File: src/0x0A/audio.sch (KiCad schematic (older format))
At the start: 2 parts

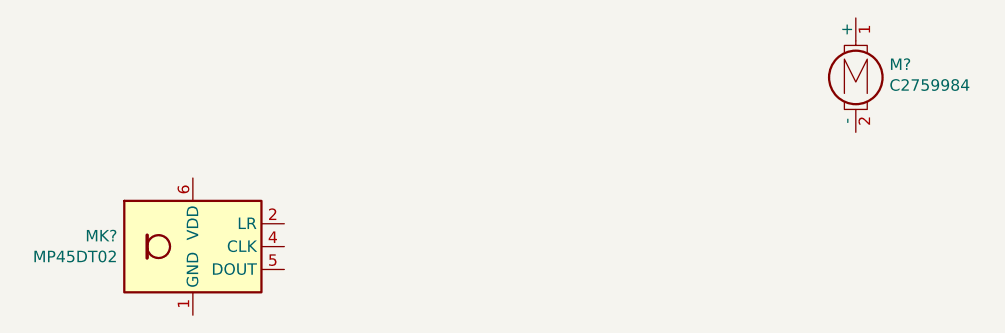
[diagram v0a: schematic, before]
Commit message: new file:   imgs/better.png 	modified:   src/0x0A/0x0A-cache.lib 	modified:   src/0x0A/0x0A.sch 	modified:   src/0x0A/antenna.sch 	modified:   src/0x0A/audio.sch 	modified:   src/0x0A/buttons.sch 	new file:   src/0x0A/cameras.sch 	modified:   src/0x0A/display.sch 	modified:   src/0x0A/gpio.sch 	modified:   src/0x0A/pwr.sch 	modified:   src/0x0A/sensors.sch 	modified:   src/0x0A/sim.sch 	modified:   src/0x0A/uart.sch 	modified:   src/0x0A/usb.sch 	new file:   src/models/body.obj 	new file:   src/models/phone.FCStd 	new file:   src/models/screen.obj
Added 3D models, integrated front & rear cameras, flash light, reformatting & more
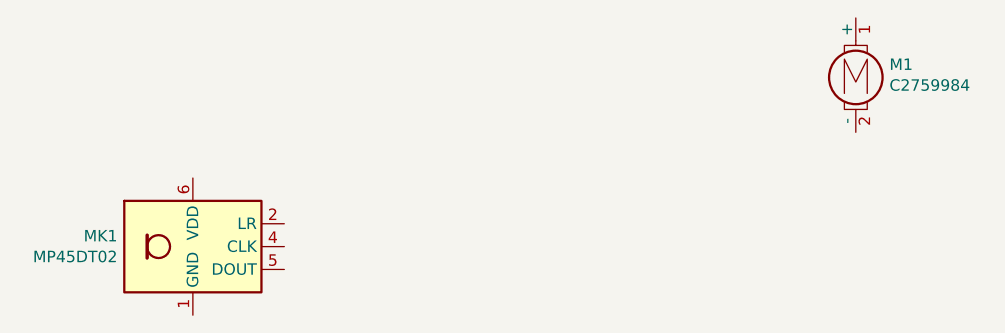
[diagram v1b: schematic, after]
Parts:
- gave numbers to parts that had none: 2
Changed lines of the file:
@@
 $Descr A4 11693 8268
 encoding utf-8
-Sheet 9 12
+Sheet 9 13
 Title "0x0A SmartPhone"
 Date "2022-09-01"
 Rev "1"
 Comp "HackThisPhone.com"
-Comment1 ""
+Comment1 "Designed By @NoahGWood for"
 Comment2 ""
 Comment3 ""
@@
 $EndDescr
 $Comp
-L Sensor_Audio:MP45DT02 MK?
+L Sensor_Audio:MP45DT02 MK1
 U 1 1 63F66D5E
 P 4050 3350
-F 0 "MK?" H 3720 3396 50  0000 R CNN
+F 0 "MK1" H 3720 3396 50  0000 R CNN
 F 1 "MP45DT02" H 3720 3305 50  0000 R CNN
 F 2 "Sensor_Audio:ST_HLGA-6_3.76x4.72mm_P1.65mm" H 3150 3000 50  0001 L CIN
@@
 $EndComp
 $Comp
-L Motor:Motor_DC_ALT M?
+L Motor:Motor_DC_ALT M1
 U 1 1 63FA151C
 P 6950 2550
-F 0 "M?" H 7097 2546 50  0000 L CNN
+F 0 "M1" H 7097 2546 50  0000 L CNN
 F 1 "C2759984" H 7097 2455 50  0000 L CNN
 F 2 "" H 6950 2460 50  0001 C CNN

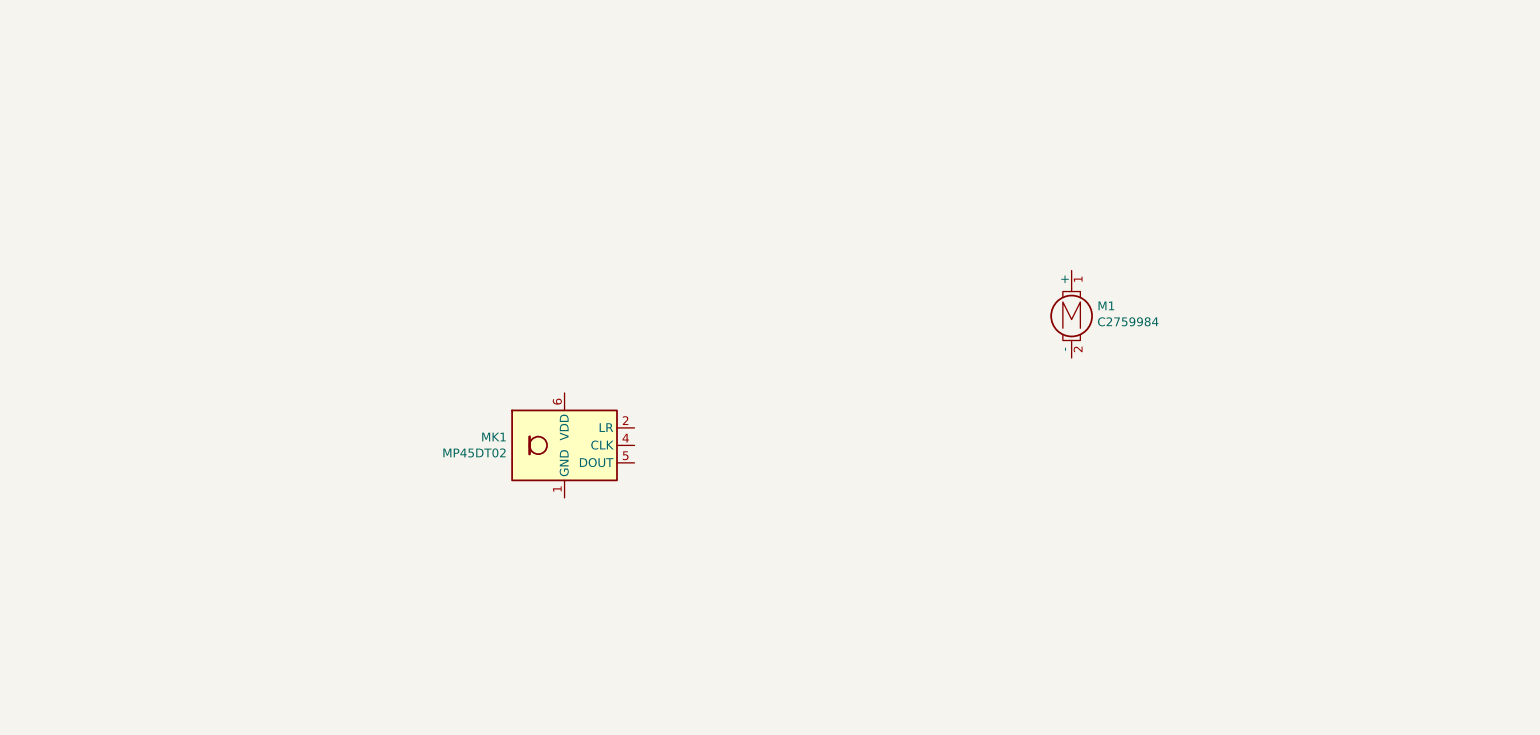
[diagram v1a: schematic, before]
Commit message: Updated schematics, started working on board layout
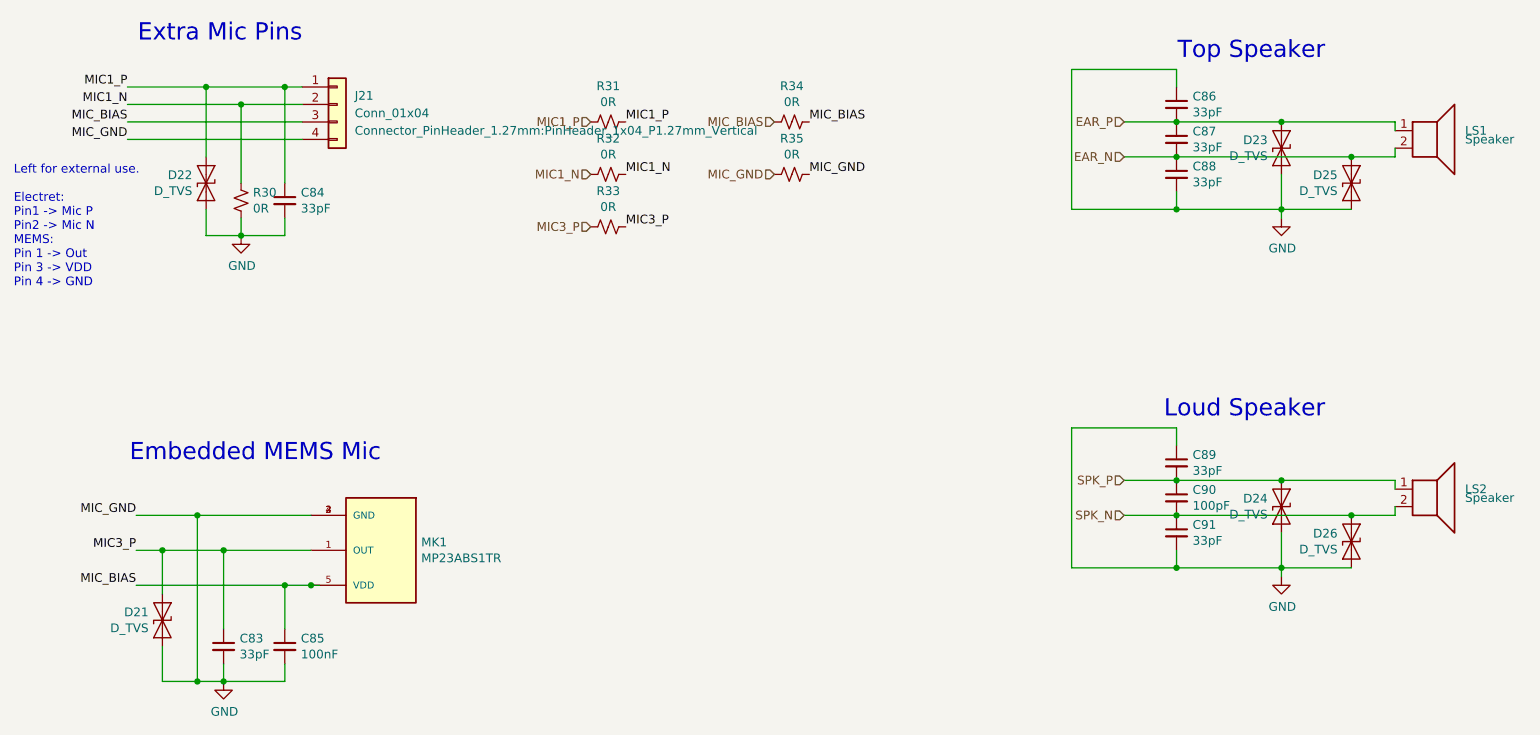
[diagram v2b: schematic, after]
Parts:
- removed M1: C2759984, symbol Motor:Motor_DC_ALT
- removed MK1: MP45DT02, Sensor_Audio:ST_HLGA-6_3.76x4.72mm_P1.65mm, symbol Sensor_Audio:MP45DT02
- added C83, C84, C86, C87, C88, C89, C91: 33pF, Capacitor_SMD:C_0603_1608Metric, symbol Device:C_Small
- added C85: 100nF, Capacitor_SMD:C_0402_1005Metric, symbol Device:C_Small
- added C90: 100pF, Capacitor_SMD:C_0603_1608Metric, symbol Device:C_Small
- added D21, D22, D23, D24, D25, D26: D_TVS, symbol Device:D_TVS
- added J21: Conn_01x04, Connector_PinHeader_1.27mm:PinHeader_1x04_P1.27mm_Vertical, symbol Connector_Generic:Conn_01x04
- added LS1, LS2: Speaker, Connector_PinHeader_1.27mm:PinHeader_1x02_P1.27mm_Horizontal, symbol Device:Speaker
- added MK1: MP23ABS1TR, SnapEDA Library:MIC_MP23ABS1TR, symbol MP23ABS1TR:MP23ABS1TR
- added R30, R31, R32, R33, R34, R35: 0R, Resistor_SMD:R_0402_1005Metric, symbol Device:R_Small_US
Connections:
- new net EAR_N: C87.2, C88.1, D25.2 (A2), LS1.2
- new net EAR_P: C86.2, C87.1, D23.2 (A2), LS1.1
- new net GND: C83.2, C84.2, C85.2, C86.1, C88.2, C89.1, C91.2, D21.1 (A1), D22.1 (A1), D23.1 (A1), D24.1 (A1), D25.1 (A1), D26.1 (A1), J21.4 (Pin_4), MK1.2 (GND), MK1.3 (GND), MK1.4 (GND), R30.1, R35.1, R35.2
- new net MIC1_N: J21.2 (Pin_2), R30.2, R32.1, R32.2
- new net MIC1_P: C84.1, D22.2 (A2), J21.1 (Pin_1), R31.1, R31.2
- new net MIC3_P: C83.1, D21.2 (A2), MK1.1 (OUT), R33.1, R33.2
- new net MIC_BIAS: C85.1, J21.3 (Pin_3), MK1.5 (VDD), R34.1, R34.2
- new net SPK_N: C90.2, C91.1, D26.2 (A2), LS2.2
- new net SPK_P: C89.2, C90.1, D24.2 (A2), LS2.1
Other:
- note added: "Embedded MEMS Mic"
- note added: "Extra Mic Pins"
- note added: "Left for external use.\n\nElectret:\nPin1 -> Mic P\nPin2 -> Mic N\nMEMS:\nPin 1 -> Out\nPin 3 -> VDD\nPin 4 -> GND"
- note added: "Loud Speaker"
- note added: "Top Speaker"
